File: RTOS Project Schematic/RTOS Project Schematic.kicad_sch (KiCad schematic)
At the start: 0 parts

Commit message: Updated power rails
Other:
- sheet Power ports: added VCC_3V3_TI, VCC_5V_AUX, VCC_5V_PI; removed VCC1, VCC2, VCC3
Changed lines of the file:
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@@
       (effects (font (size 1.27 1.27)) (justify left top))
     )
-    (pin "VCC3" output (at 66.04 38.1 0)
+    (pin "VCC_5V_AUX" output (at 66.04 38.1 0)
       (effects (font (size 1.27 1.27)) (justify right))
     )
-    (pin "VCC1" output (at 66.04 30.48 0)
+    (pin "VCC_3V3_TI" output (at 66.04 30.48 0)
       (effects (font (size 1.27 1.27)) (justify right))
     )
@@
       (effects (font (size 1.27 1.27)) (justify right))
     )
-    (pin "VCC2" output (at 66.04 34.29 0)
+    (pin "VCC_5V_PI" output (at 66.04 34.29 0)
       (effects (font (size 1.27 1.27)) (justify right))
     )

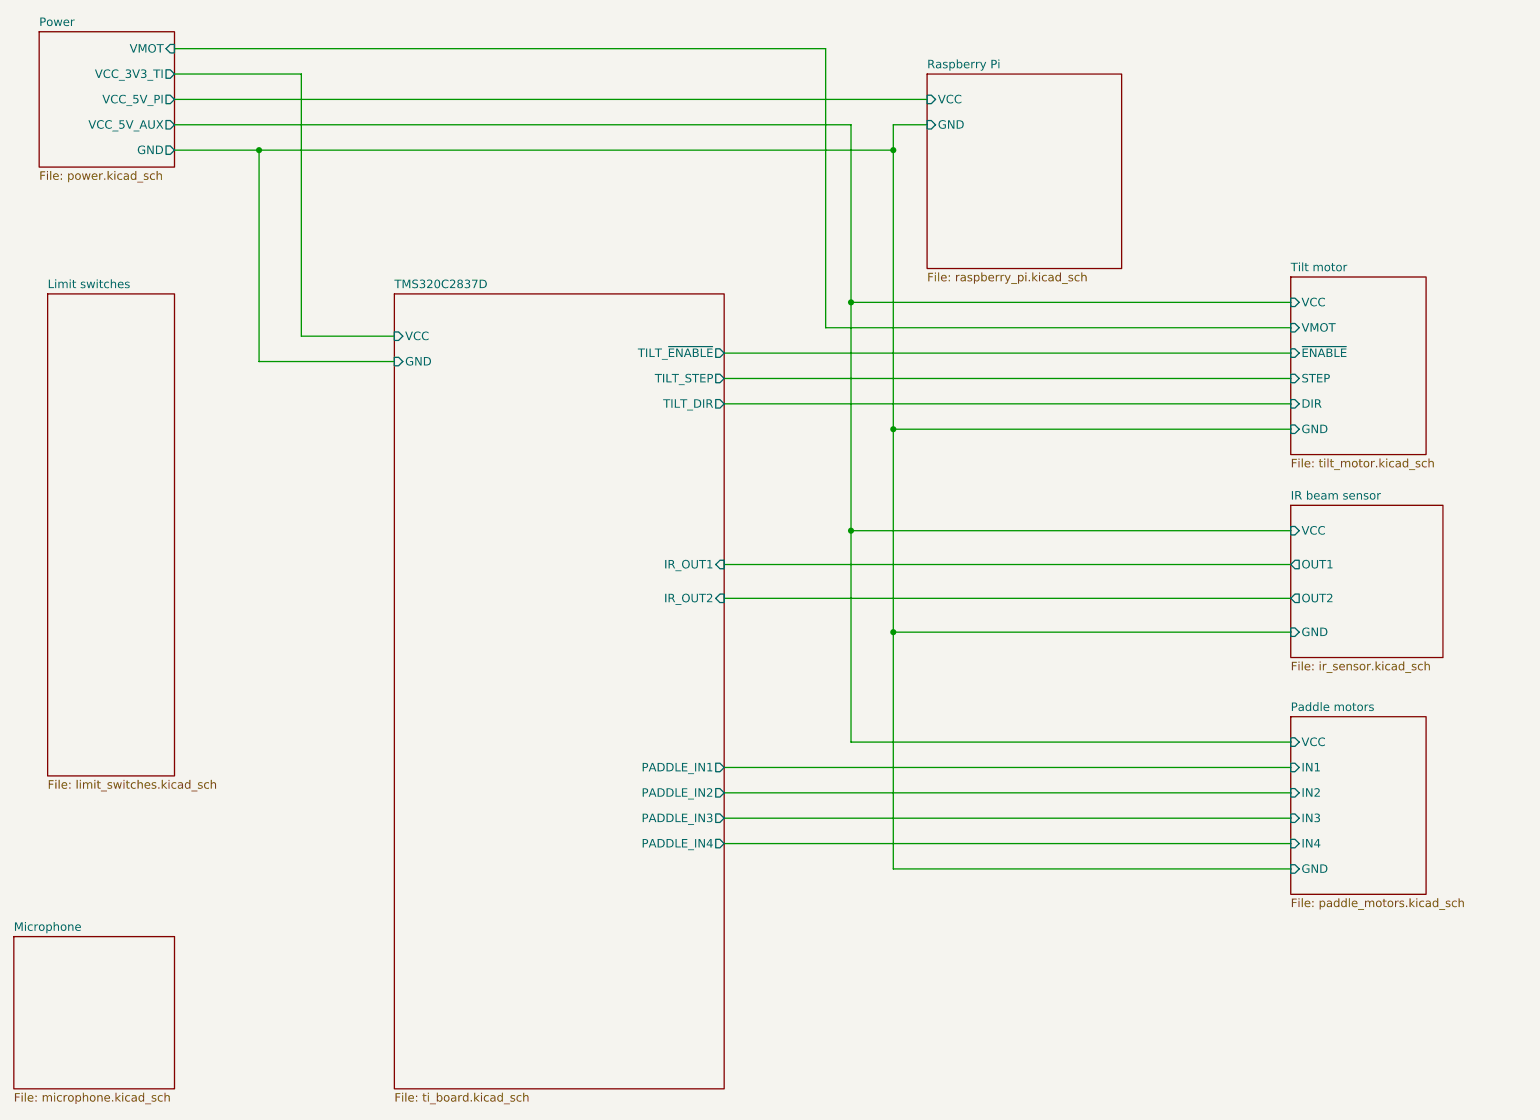
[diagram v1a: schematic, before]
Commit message: Added preliminary microphone circuit
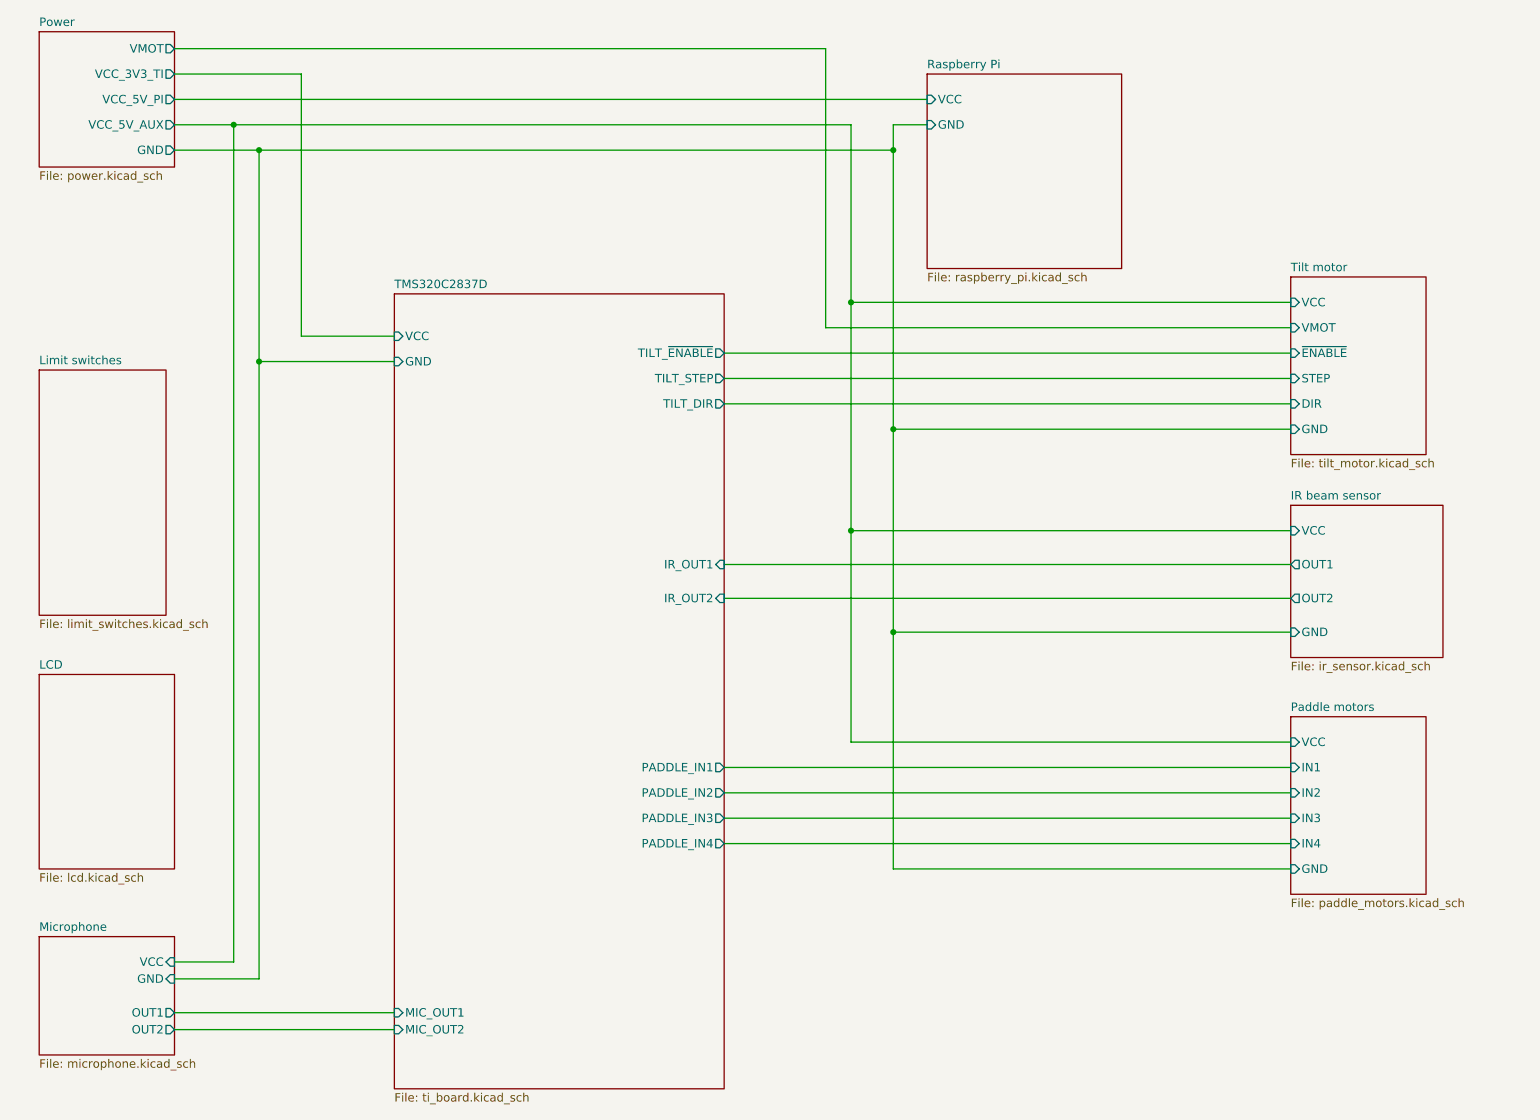
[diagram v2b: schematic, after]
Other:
- added sheet LCD (lcd.kicad_sch)
- sheet Microphone ports: added GND, OUT1, OUT2, VCC; removed none
- sheet TMS320C2837D ports: added MIC_OUT1, MIC_OUT2; removed none
- company: (none) -> Eddie and Felix
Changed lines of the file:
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@@
   (title_block
     (title "ELEX 7820 RTOS Project")
+    (date "2023-11-29")
+    (rev "A")
+    (company "Eddie and Felix")
   )
   (junction (at 173.99 83.82) (diameter 0) (color 0 0 0 0)
@@
   (junction (at 167.64 64.77) (diameter 0) (color 0 0 0 0)
   )
+  (junction (at 74.93 38.1) (diameter 0) (color 0 0 0 0)
+  )
   (junction (at 167.64 99.06) (diameter 0) (color 0 0 0 0)
   )
@@
   (junction (at 78.74 41.91) (diameter 0) (color 0 0 0 0)
   )
-  (wire (pts (xy 66.04 38.1) (xy 167.64 38.1))
+  (junction (at 78.74 73.66) (diameter 0) (color 0 0 0 0)
+  )
+  (wire (pts (xy 66.04 38.1) (xy 74.93 38.1))
+    (stroke (width 0) (type default))
+  )
+  (wire (pts (xy 66.04 173.99) (xy 99.06 173.99))
     (stroke (width 0) (type default))
   )
@@
     (stroke (width 0) (type default))
   )
+  (wire (pts (xy 74.93 163.83) (xy 74.93 38.1))
+    (stroke (width 0) (type default))
+  )
   (wire (pts (xy 173.99 41.91) (xy 173.99 83.82))
     (stroke (width 0) (type default))
@@
     (stroke (width 0) (type default))
   )
+  (wire (pts (xy 74.93 38.1) (xy 167.64 38.1))
+    (stroke (width 0) (type default))
+  )
   (wire (pts (xy 66.04 26.67) (xy 163.83 26.67))
     (stroke (width 0) (type default))
@@
     (stroke (width 0) (type default))
   )
+  (wire (pts (xy 66.04 166.37) (xy 78.74 166.37))
+    (stroke (width 0) (type default))
+  )
+  (wire (pts (xy 66.04 163.83) (xy 74.93 163.83))
+    (stroke (width 0) (type default))
+  )
   (wire (pts (xy 167.64 64.77) (xy 233.68 64.77))
     (stroke (width 0) (type default))
@@
     (stroke (width 0) (type default))
   )
+  (wire (pts (xy 78.74 166.37) (xy 78.74 73.66))
+    (stroke (width 0) (type default))
+  )
+  (wire (pts (xy 66.04 171.45) (xy 99.06 171.45))
+    (stroke (width 0) (type default))
+  )
   (wire (pts (xy 173.99 38.1) (xy 179.07 38.1))
     (stroke (width 0) (type default))
@@
     (stroke (width 0) (type default))
   )
+  (sheet (at 45.72 120.65) (size 20.32 29.21) (fields_autoplaced)
+    (stroke (width 0.1524) (type solid))
+    (fill (color 0 0 0 0.0000))
+    (property "Sheetname" "LCD" (at 45.72 119.9384 0)
+      (effects (font (size 1.27 1.27)) (justify left bottom))
+    )
+    (property "Sheetfile" "lcd.kicad_sch" (at 45.72 150.4446 0)
+      (effects (font (size 1.27 1.27)) (justify left top))
+    )
+    (instances
+      (project "RTOS Project Schematic"
+        (path "/c6d2ace8-9811-4d31-9242-ec8aa6e12e77" (page "10"))
+      )
+    )
+  )
   (sheet (at 99.06 63.5) (size 49.53 119.38) (fields_autoplaced)
     (stroke (width 0.1524) (type solid))
@@
       (effects (font (size 1.27 1.27)) (justify right))
     )
+    (pin "MIC_OUT1" input (at 99.06 171.45 180)
+      (effects (font (size 1.27 1.27)) (justify left))
+    )
+    (pin "MIC_OUT2" input (at 99.06 173.99 180)
+      (effects (font (size 1.27 1.27)) (justify left))
+    )
     (instances
       (project "RTOS Project Schematic"
@@
     )
   )
-  (sheet (at 46.99 63.5) (size 19.05 72.39) (fields_autoplaced)
-    (stroke (width 0.1524) (type solid))
-    (fill (color 0 0 0 0.0000))
-    (property "Sheetname" "Limit switches" (at 46.99 62.7884 0)
-      (effects (font (size 1.27 1.27)) (justify left bottom))
-    )
-    (property "Sheetfile" "limit_switches.kicad_sch" (at 46.99 136.4746 0)
+  (sheet (at 45.72 74.93) (size 19.05 36.83) (fields_autoplaced)
+    (stroke (width 0.1524) (type solid))
+    (fill (color 0 0 0 0.0000))
+    (property "Sheetname" "Limit switches" (at 45.72 74.2184 0)
+      (effects (font (size 1.27 1.27)) (justify left bottom))
+    )
+    (property "Sheetfile" "limit_switches.kicad_sch" (at 45.72 112.3446 0)
       (effects (font (size 1.27 1.27)) (justify left top))
     )
@@
     )
   )
-  (sheet (at 41.91 160.02) (size 24.13 22.86) (fields_autoplaced)
-    (stroke (width 0.1524) (type solid))
-    (fill (color 0 0 0 0.0000))
-    (property "Sheetname" "Microphone" (at 41.91 159.3084 0)
-      (effects (font (size 1.27 1.27)) (justify left bottom))
-    )
-    (property "Sheetfile" "microphone.kicad_sch" (at 41.91 183.4646 0)
-      (effects (font (size 1.27 1.27)) (justify left top))
+  (sheet (at 45.72 160.02) (size 20.32 17.78) (fields_autoplaced)
+    (stroke (width 0.1524) (type solid))
+    (fill (color 0 0 0 0.0000))
+    (property "Sheetname" "Microphone" (at 45.72 159.3084 0)
+      (effects (font (size 1.27 1.27)) (justify left bottom))
+    )
+    (property "Sheetfile" "microphone.kicad_sch" (at 45.72 178.3846 0)
+      (effects (font (size 1.27 1.27)) (justify left top))
+    )
+    (pin "GND" input (at 66.04 166.37 0)
+      (effects (font (size 1.27 1.27)) (justify right))
+    )
+    (pin "VCC" input (at 66.04 163.83 0)
+      (effects (font (size 1.27 1.27)) (justify right))
+    )
+    (pin "OUT1" output (at 66.04 171.45 0)
+      (effects (font (size 1.27 1.27)) (justify right))
+    )
+    (pin "OUT2" output (at 66.04 173.99 0)
+      (effects (font (size 1.27 1.27)) (justify right))
     )
     (instances
@@
       (effects (font (size 1.27 1.27)) (justify right))
     )
-    (pin "VMOT" input (at 66.04 26.67 0)
-      (effects (font (size 1.27 1.27)) (justify right))
-    )
+    (pin "VMOT" output (at 66.04 26.67 0)
+      (effects (font (size 1.27 1.27)) (justify right))
+    )

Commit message: Updated schematics
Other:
- sheet TMS320C2837D renamed LAUNCHXL-F28379D
- sheet LAUNCHXL-F28379D ports: added LIMIT_SW1_AL, LIMIT_SW2_AR, LIMIT_SW3_P1L, LIMIT_SW4_P1R, LIMIT_SW5_P2L, LIMIT_SW6_P2R, PI_SPI-CLK, PI_SPI_CS, PI_SPI_MOSI, PI_SPI_SIMO; removed none
- sheet Limit switches ports: added GND, SW1_AL, SW2_AR, SW3_P1L, SW4_P1R, SW5_P2L, SW6_P2R; removed none
- sheet Raspberry Pi ports: added SPI_CLK, SPI_CS, SPI_MOSI, SPI_SIMO; removed none
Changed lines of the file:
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@@
   (junction (at 74.93 38.1) (diameter 0) (color 0 0 0 0)
   )
-  (junction (at 167.64 99.06) (diameter 0) (color 0 0 0 0)
+  (junction (at 85.09 30.48) (diameter 0) (color 0 0 0 0)
   )
   (junction (at 173.99 114.3) (diameter 0) (color 0 0 0 0)
@@
   (junction (at 173.99 41.91) (diameter 0) (color 0 0 0 0)
   )
+  (junction (at 78.74 78.74) (diameter 0) (color 0 0 0 0)
+  )
   (junction (at 78.74 41.91) (diameter 0) (color 0 0 0 0)
   )
@@
     (stroke (width 0) (type default))
   )
+  (wire (pts (xy 64.77 95.25) (xy 99.06 95.25))
+    (stroke (width 0) (type default))
+  )
   (wire (pts (xy 173.99 38.1) (xy 173.99 41.91))
     (stroke (width 0) (type default))
   )
+  (wire (pts (xy 125.73 63.5) (xy 125.73 48.26))
+    (stroke (width 0) (type default))
+  )
   (wire (pts (xy 167.64 38.1) (xy 167.64 64.77))
     (stroke (width 0) (type default))
@@
     (stroke (width 0) (type default))
   )
+  (wire (pts (xy 64.77 78.74) (xy 78.74 78.74))
+    (stroke (width 0) (type default))
+  )
   (wire (pts (xy 233.68 149.86) (xy 173.99 149.86))
     (stroke (width 0) (type default))
   )
+  (wire (pts (xy 123.19 45.72) (xy 179.07 45.72))
+    (stroke (width 0) (type default))
+  )
   (wire (pts (xy 148.59 146.05) (xy 233.68 146.05))
     (stroke (width 0) (type default))
   )
+  (wire (pts (xy 233.68 99.06) (xy 160.02 99.06))
+    (stroke (width 0) (type default))
+  )
   (wire (pts (xy 233.68 130.81) (xy 167.64 130.81))
     (stroke (width 0) (type default))
@@
     (stroke (width 0) (type default))
   )
+  (wire (pts (xy 78.74 78.74) (xy 78.74 73.66))
+    (stroke (width 0) (type default))
+  )
   (wire (pts (xy 173.99 41.91) (xy 173.99 83.82))
     (stroke (width 0) (type default))
@@
     (stroke (width 0) (type default))
   )
+  (wire (pts (xy 160.02 30.48) (xy 85.09 30.48))
+    (stroke (width 0) (type default))
+  )
   (wire (pts (xy 148.59 104.14) (xy 233.68 104.14))
     (stroke (width 0) (type default))
@@
     (stroke (width 0) (type default))
   )
+  (wire (pts (xy 130.81 53.34) (xy 179.07 53.34))
+    (stroke (width 0) (type default))
+  )
   (wire (pts (xy 66.04 34.29) (xy 179.07 34.29))
     (stroke (width 0) (type default))
   )
+  (wire (pts (xy 128.27 50.8) (xy 179.07 50.8))
+    (stroke (width 0) (type default))
+  )
+  (wire (pts (xy 160.02 99.06) (xy 160.02 30.48))
+    (stroke (width 0) (type default))
+  )
   (wire (pts (xy 148.59 138.43) (xy 233.68 138.43))
     (stroke (width 0) (type default))
@@
     (stroke (width 0) (type default))
   )
+  (wire (pts (xy 64.77 99.06) (xy 99.06 99.06))
+    (stroke (width 0) (type default))
+  )
+  (wire (pts (xy 64.77 102.87) (xy 99.06 102.87))
+    (stroke (width 0) (type default))
+  )
   (wire (pts (xy 148.59 134.62) (xy 233.68 134.62))
     (stroke (width 0) (type default))
@@
     (stroke (width 0) (type default))
   )
-  (wire (pts (xy 233.68 99.06) (xy 167.64 99.06))
-    (stroke (width 0) (type default))
-  )
-  (wire (pts (xy 167.64 64.77) (xy 167.64 99.06))
+  (wire (pts (xy 64.77 91.44) (xy 99.06 91.44))
+    (stroke (width 0) (type default))
+  )
+  (wire (pts (xy 167.64 64.77) (xy 167.64 130.81))
     (stroke (width 0) (type default))
   )
@@
     (stroke (width 0) (type default))
   )
+  (wire (pts (xy 125.73 48.26) (xy 179.07 48.26))
+    (stroke (width 0) (type default))
+  )
   (wire (pts (xy 66.04 166.37) (xy 78.74 166.37))
     (stroke (width 0) (type default))
   )
+  (wire (pts (xy 64.77 87.63) (xy 99.06 87.63))
+    (stroke (width 0) (type default))
+  )
   (wire (pts (xy 66.04 163.83) (xy 74.93 163.83))
     (stroke (width 0) (type default))
@@
     (stroke (width 0) (type default))
   )
-  (wire (pts (xy 78.74 166.37) (xy 78.74 73.66))
+  (wire (pts (xy 78.74 166.37) (xy 78.74 78.74))
     (stroke (width 0) (type default))
   )
@@
     (stroke (width 0) (type default))
   )
+  (wire (pts (xy 64.77 106.68) (xy 99.06 106.68))
+    (stroke (width 0) (type default))
+  )
+  (wire (pts (xy 123.19 63.5) (xy 123.19 45.72))
+    (stroke (width 0) (type default))
+  )
   (wire (pts (xy 173.99 38.1) (xy 179.07 38.1))
     (stroke (width 0) (type default))
   )
+  (wire (pts (xy 128.27 63.5) (xy 128.27 50.8))
+    (stroke (width 0) (type default))
+  )
   (wire (pts (xy 78.74 73.66) (xy 99.06 73.66))
     (stroke (width 0) (type default))
   )
+  (wire (pts (xy 130.81 63.5) (xy 130.81 53.34))
+    (stroke (width 0) (type default))
+  )
   (wire (pts (xy 148.59 109.22) (xy 233.68 109.22))
     (stroke (width 0) (type default))
   )
-  (wire (pts (xy 167.64 99.06) (xy 167.64 130.81))
-    (stroke (width 0) (type default))
-  )
   (wire (pts (xy 85.09 30.48) (xy 85.09 69.85))
     (stroke (width 0) (type default))
@@
     (stroke (width 0.1524) (type solid))
     (fill (color 0 0 0 0.0000))
-    (property "Sheetname" "TMS320C2837D" (at 99.06 62.7884 0)
+    (property "Sheetname" "LAUNCHXL-F28379D" (at 99.06 62.7884 0)
       (effects (font (size 1.27 1.27)) (justify left bottom))
     )
@@
       (effects (font (size 1.27 1.27)) (justify left))
     )
+    (pin "LIMIT_SW6_P2R" input (at 99.06 106.68 180)
+      (effects (font (size 1.27 1.27)) (justify left))
+    )
+    (pin "LIMIT_SW4_P1R" input (at 99.06 99.06 180)
+      (effects (font (size 1.27 1.27)) (justify left))
+    )
+    (pin "LIMIT_SW5_P2L" input (at 99.06 102.87 180)
+      (effects (font (size 1.27 1.27)) (justify left))
+    )
+    (pin "LIMIT_SW1_AL" input (at 99.06 87.63 180)
+      (effects (font (size 1.27 1.27)) (justify left))
+    )
+    (pin "LIMIT_SW2_AR" input (at 99.06 91.44 180)
+      (effects (font (size 1.27 1.27)) (justify left))
+    )
+    (pin "LIMIT_SW3_P1L" input (at 99.06 95.25 180)
+      (effects (font (size 1.27 1.27)) (justify left))
+    )
+    (pin "PI_SPI-CLK" bidirectional (at 123.19 63.5 90)
+      (effects (font (size 1.27 1.27)) (justify right))
+    )
+    (pin "PI_SPI_CS" bidirectional (at 125.73 63.5 90)
+      (effects (font (size 1.27 1.27)) (justify right))
+    )
+    (pin "PI_SPI_SIMO" bidirectional (at 128.27 63.5 90)
+      (effects (font (size 1.27 1.27)) (justify right))
+    )
+    (pin "PI_SPI_MOSI" bidirectional (at 130.81 63.5 90)
+      (effects (font (size 1.27 1.27)) (justify right))
+    )
     (instances
       (project "RTOS Project Schematic"
@@
       (effects (font (size 1.27 1.27)) (justify left top))
     )
+    (pin "GND" input (at 64.77 78.74 0)
+      (effects (font (size 1.27 1.27)) (justify right))
+    )
+    (pin "SW6_P2R" output (at 64.77 106.68 0)
+      (effects (font (size 1.27 1.27)) (justify right))
+    )
+    (pin "SW1_AL" output (at 64.77 87.63 0)
+      (effects (font (size 1.27 1.27)) (justify right))
+    )
+    (pin "SW2_AR" output (at 64.77 91.44 0)
+      (effects (font (size 1.27 1.27)) (justify right))
+    )
+    (pin "SW3_P1L" output (at 64.77 95.25 0)
+      (effects (font (size 1.27 1.27)) (justify right))
+    )
+    (pin "SW4_P1R" output (at 64.77 99.06 0)
+      (effects (font (size 1.27 1.27)) (justify right))
+    )
+    (pin "SW5_P2L" output (at 64.77 102.87 0)
+      (effects (font (size 1.27 1.27)) (justify right))
+    )
     (instances
       (project "RTOS Project Schematic"
@@
       (effects (font (size 1.27 1.27)) (justify left))
     )
+    (pin "SPI_SIMO" bidirectional (at 179.07 50.8 180)
+      (effects (font (size 1.27 1.27)) (justify left))
+    )
+    (pin "SPI_CLK" bidirectional (at 179.07 45.72 180)
+      (effects (font (size 1.27 1.27)) (justify left))
+    )
+    (pin "SPI_MOSI" bidirectional (at 179.07 53.34 180)
+      (effects (font (size 1.27 1.27)) (justify left))
+    )
+    (pin "SPI_CS" bidirectional (at 179.07 48.26 180)
+      (effects (font (size 1.27 1.27)) (justify left))
+    )
